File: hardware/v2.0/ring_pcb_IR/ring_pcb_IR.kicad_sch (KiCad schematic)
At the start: 18 parts, among them Q1 Q_PNP_BEC, Q2 Q_Dual_NPN_NPN_C2E2C1E1B1B2, Q3 Q_Dual_NPN_NPN_C2E2C1E1B1B2, U2 ATtiny85-20M

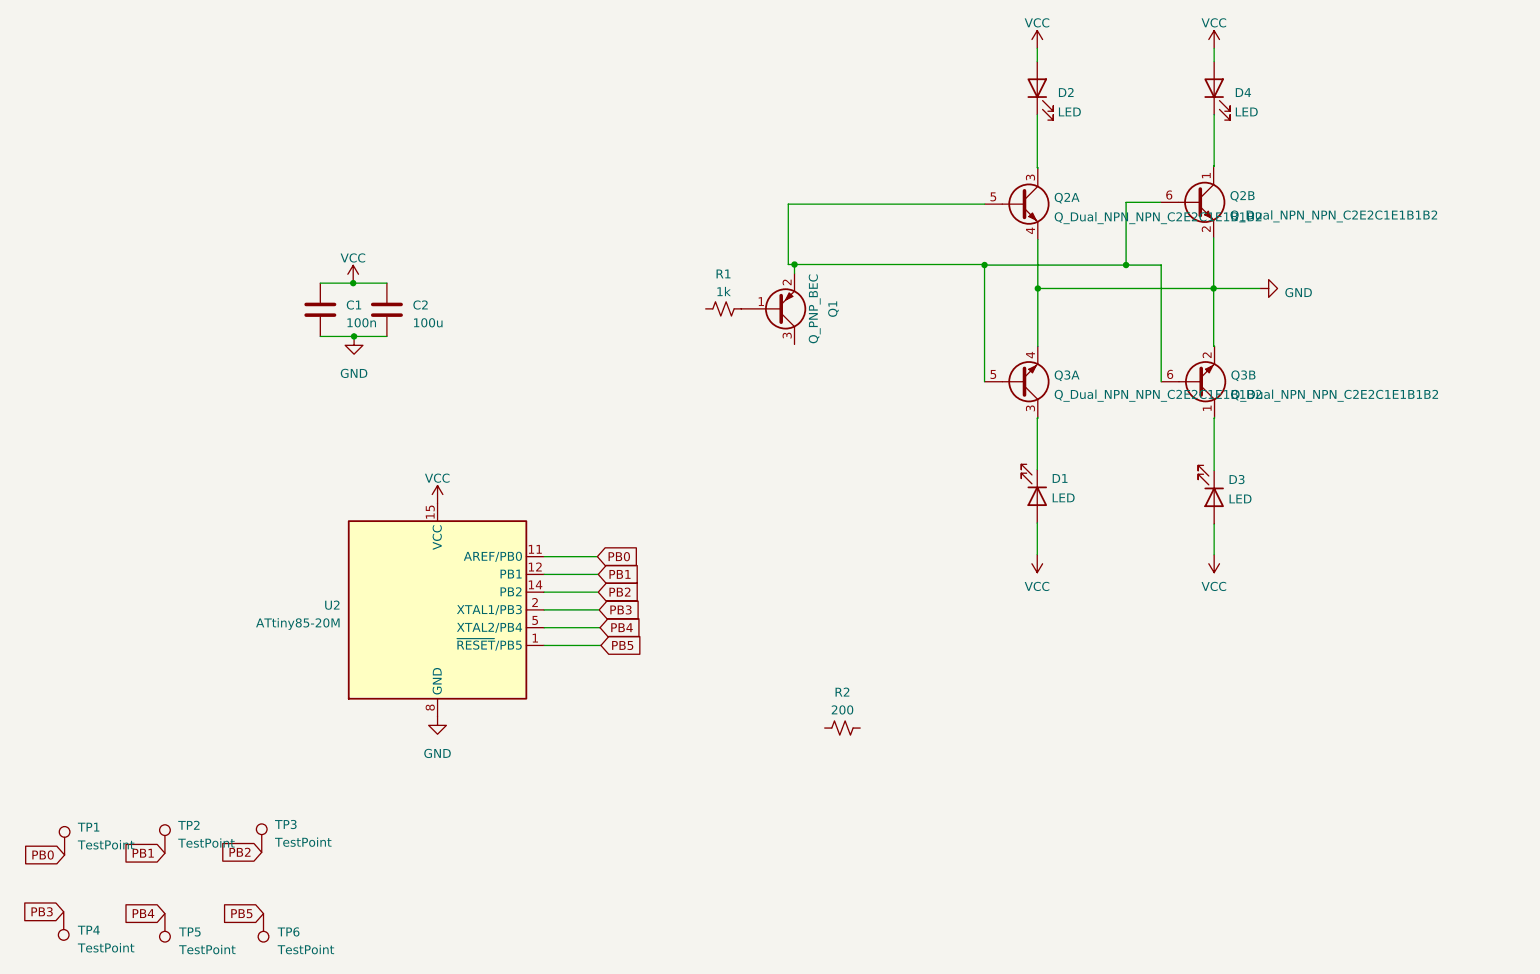
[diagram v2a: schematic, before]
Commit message: Add more wiring for LED and power pads
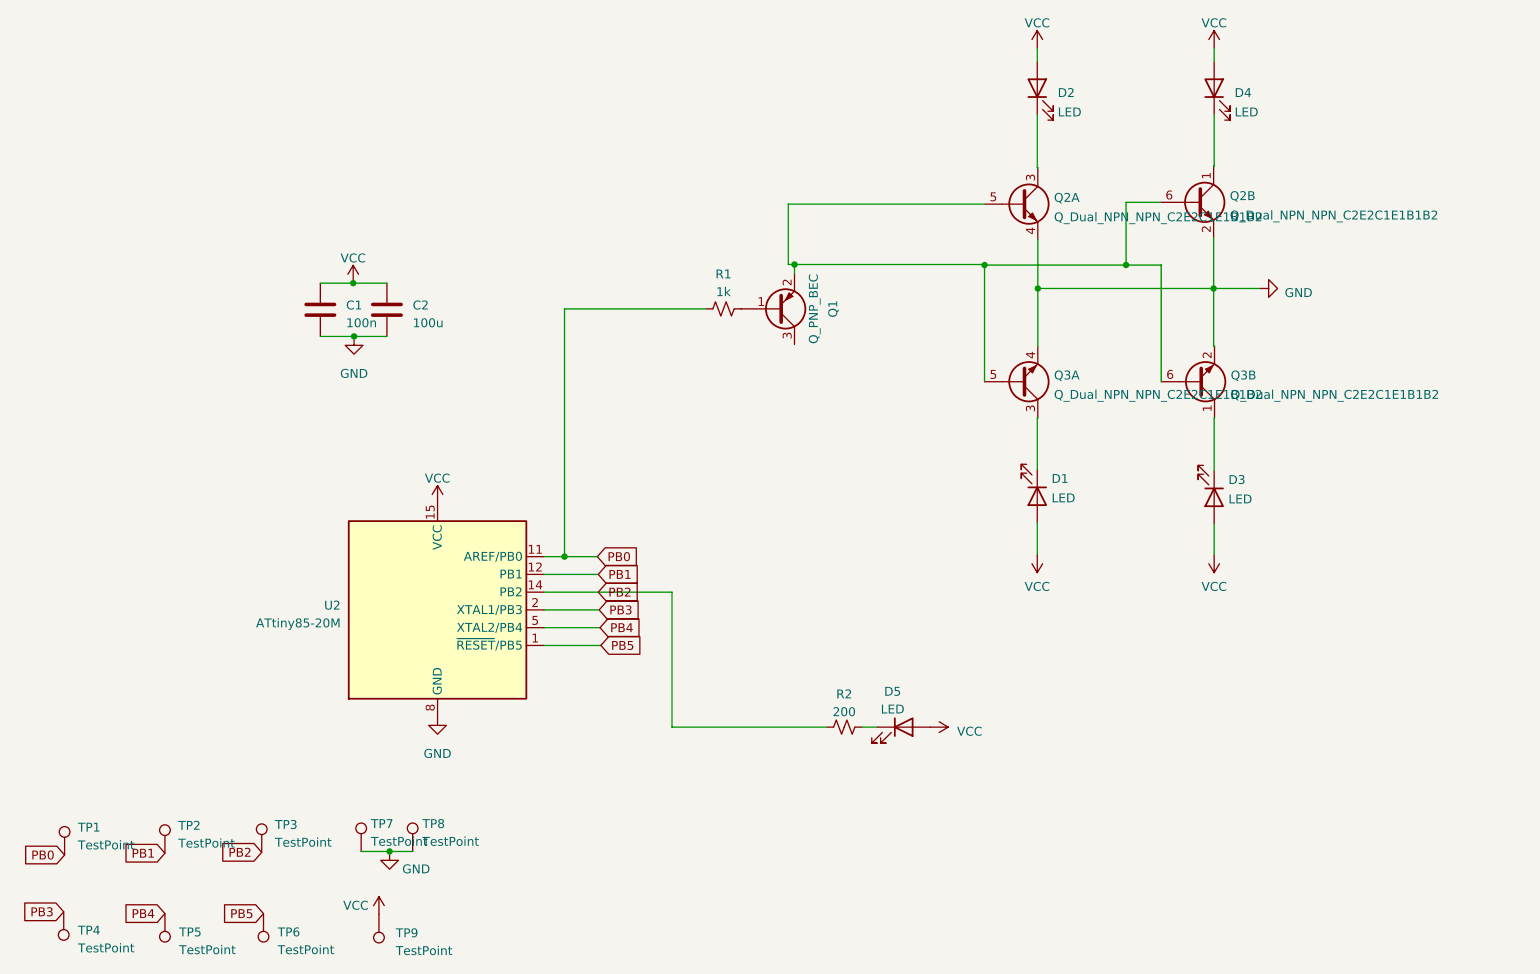
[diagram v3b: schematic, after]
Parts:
- added D5: LED, LED_SMD:LED_0603_1608Metric, symbol Device:LED
- added TP7, TP8, TP9: TestPoint, TestPoint:TestPoint_Pad_1.0x1.0mm, symbol Connector:TestPoint
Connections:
- net GND: now also TP7.1, TP8.1
- net PB0: now also R1.1
- net PB2: now also R2.2
- net VCC: now also D5.2 (A), TP9.1
- net at R2.1: now also D5.1 (K)
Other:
- moved on the sheet: R2
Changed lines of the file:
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@@
   (junction (at 100.33 57.15) (diameter 0) (color 0 0 0 0)
   )
+  (junction (at 105.537 138.43) (diameter 0) (color 0 0 0 0)
+  )
   (junction (at 100.457 64.77) (diameter 0) (color 0 0 0 0)
   )
@@
   (junction (at 163.449 54.483) (diameter 0) (color 0 0 0 0)
   )
+  (junction (at 130.556 96.266) (diameter 0) (color 0 0 0 0)
+  )
   (wire (pts (xy 198.247 40.64) (xy 198.247 40.767))
     (stroke (width 0) (type default))
@@
     (stroke (width 0) (type default))
   )
+  (wire (pts (xy 173.101 120.65) (xy 175.26 120.65))
+    (stroke (width 0) (type default))
+  )
   (wire (pts (xy 223.4692 76.454) (xy 223.4692 83.9724))
     (stroke (width 0) (type default))
@@
     (stroke (width 0) (type default))
   )
-  (wire (pts (xy 127.635 101.346) (xy 135.382 101.346))
+  (wire (pts (xy 127.635 101.346) (xy 145.923 101.346))
+    (stroke (width 0) (type default))
+  )
+  (wire (pts (xy 130.556 96.266) (xy 135.255 96.266))
     (stroke (width 0) (type default))
   )
@@
     (stroke (width 0) (type default))
   )
+  (wire (pts (xy 130.556 60.833) (xy 130.556 96.266))
+    (stroke (width 0) (type default))
+  )
   (wire (pts (xy 127.635 98.806) (xy 135.382 98.806))
     (stroke (width 0) (type default))
@@
     (stroke (width 0) (type default))
   )
-  (wire (pts (xy 127.635 96.266) (xy 135.255 96.266))
+  (wire (pts (xy 127.635 96.266) (xy 130.556 96.266))
     (stroke (width 0) (type default))
   )
@@
     (stroke (width 0) (type default))
   )
+  (wire (pts (xy 168.021 120.65) (xy 145.923 120.65))
+    (stroke (width 0) (type default))
+  )
   (wire (pts (xy 210.8708 54.5592) (xy 190.627 54.5592))
     (stroke (width 0) (type default))
@@
     (stroke (width 0) (type default))
   )
+  (wire (pts (xy 101.473 138.43) (xy 105.537 138.43))
+    (stroke (width 0) (type default))
+  )
+  (wire (pts (xy 145.923 120.65) (xy 145.923 101.346))
+    (stroke (width 0) (type default))
+  )
   (wire (pts (xy 210.8708 45.593) (xy 210.8708 54.5592))
     (stroke (width 0) (type default))
@@
     (stroke (width 0) (type default))
   )
+  (wire (pts (xy 150.749 60.833) (xy 130.556 60.833))
+    (stroke (width 0) (type default))
+  )
   (wire (pts (xy 223.4692 23.5712) (xy 223.4692 25.4508))
     (stroke (width 0) (type default))
@@
   )
   (wire (pts (xy 198.247 76.327) (xy 198.247 76.454))
+    (stroke (width 0) (type default))
+  )
+  (wire (pts (xy 105.537 138.43) (xy 108.839 138.43))
     (stroke (width 0) (type default))
   )
@@
     )
   )
+  (symbol (lib_id "Connector:TestPoint") (at 108.839 138.43 0) (unit 1)
+    (in_bom yes) (on_board yes) (dnp no) (fields_autoplaced)
+    (property "Reference" "TP8" (at 110.236 134.493 0)
+      (effects (font (size 1.27 1.27)) (justify left))
+    )
+    (property "Value" "TestPoint" (at 110.236 137.033 0)
+      (effects (font (size 1.27 1.27)) (justify left))
+    )
+    (property "Footprint" "TestPoint:TestPoint_Pad_1.0x1.0mm" (at 113.919 138.43 0)
+      (effects (font (size 1.27 1.27)) hide)
+    )
+    (property "Datasheet" "~" (at 113.919 138.43 0)
+      (effects (font (size 1.27 1.27)) hide)
+    )
+    (pin "1")
+    (instances
+      (project "ring_pcb_IR"
+        (path "/e63e39d7-6ac0-4ffd-8aa3-1841a4541b55"
+          (reference "TP8") (unit 1)
+        )
+      )
+    )
+  )
   (symbol (lib_id "Connector:TestPoint") (at 87.503 147.32 180) (unit 1)
     (in_bom yes) (on_board yes) (dnp no) (fields_autoplaced)
@@
         (path "/e63e39d7-6ac0-4ffd-8aa3-1841a4541b55"
           (reference "TP6") (unit 1)
+        )
+      )
+    )
+  )
+  (symbol (lib_id "Device:LED") (at 179.07 120.65 0) (unit 1)
+    (in_bom yes) (on_board yes) (dnp no) (fields_autoplaced)
+    (property "Reference" "D5" (at 177.4825 115.57 0)
+      (effects (font (size 1.27 1.27)))
+    )
+    (property "Value" "LED" (at 177.4825 118.11 0)
+      (effects (font (size 1.27 1.27)))
+    )
+    (property "Footprint" "LED_SMD:LED_0603_1608Metric" (at 179.07 120.65 0)
+      (effects (font (size 1.27 1.27)) hide)
+    )
+    (property "Datasheet" "~" (at 179.07 120.65 0)
+      (effects (font (size 1.27 1.27)) hide)
+    )
+    (pin "1")
+    (pin "2")
+    (instances
+      (project "ring_pcb_IR"
+        (path "/e63e39d7-6ac0-4ffd-8aa3-1841a4541b55"
+          (reference "D5") (unit 1)
+        )
+      )
+    )
+  )
+  (symbol (lib_id "Connector:TestPoint") (at 101.473 138.43 0) (unit 1)
+    (in_bom yes) (on_board yes) (dnp no) (fields_autoplaced)
+    (property "Reference" "TP7" (at 102.87 134.493 0)
+      (effects (font (size 1.27 1.27)) (justify left))
+    )
+    (property "Value" "TestPoint" (at 102.87 137.033 0)
+      (effects (font (size 1.27 1.27)) (justify left))
+    )
+    (property "Footprint" "TestPoint:TestPoint_Pad_1.0x1.0mm" (at 106.553 138.43 0)
+      (effects (font (size 1.27 1.27)) hide)
+    )
+    (property "Datasheet" "~" (at 106.553 138.43 0)
+      (effects (font (size 1.27 1.27)) hide)
+    )
+    (pin "1")
+    (instances
+      (project "ring_pcb_IR"
+        (path "/e63e39d7-6ac0-4ffd-8aa3-1841a4541b55"
+          (reference "TP7") (unit 1)
         )
       )
@@
     )
   )
+  (symbol (lib_id "Connector:TestPoint") (at 104.013 147.447 180) (unit 1)
+    (in_bom yes) (on_board yes) (dnp no) (fields_autoplaced)
+    (property "Reference" "TP9" (at 106.426 150.114 0)
+      (effects (font (size 1.27 1.27)) (justify right))
+    )
+    (property "Value" "TestPoint" (at 106.426 152.654 0)
+      (effects (font (size 1.27 1.27)) (justify right))
+    )
+    (property "Footprint" "TestPoint:TestPoint_Pad_1.0x1.0mm" (at 98.933 147.447 0)
+      (effects (font (size 1.27 1.27)) hide)
+    )
+    (property "Datasheet" "~" (at 98.933 147.447 0)
+      (effects (font (size 1.27 1.27)) hide)
+    )
+    (pin "1")
+    (instances
+      (project "ring_pcb_IR"
+        (path "/e63e39d7-6ac0-4ffd-8aa3-1841a4541b55"
+          (reference "TP9") (unit 1)
+        )
+      )
+    )
+  )
   (symbol (lib_id "Device:Q_Dual_NPN_NPN_C2E2C1E1B1B2") (at 220.98 71.247 0) (mirror x) (unit 2)
     (in_bom yes) (on_board yes) (dnp no) (fields_autoplaced)
@@
     )
   )
-  (symbol (lib_id "Device:R_Small_US") (at 170.307 120.777 90) (unit 1)
-    (in_bom yes) (on_board yes) (dnp no) (fields_autoplaced)
-    (property "Reference" "R2" (at 170.307 115.697 90)
-      (effects (font (size 1.27 1.27)))
-    )
-    (property "Value" "200" (at 170.307 118.237 90)
-      (effects (font (size 1.27 1.27)))
-    )
-    (property "Footprint" "Resistor_SMD:R_0603_1608Metric" (at 170.307 120.777 0)
-      (effects (font (size 1.27 1.27)) hide)
-    )
-    (property "Datasheet" "~" (at 170.307 120.777 0)
+  (symbol (lib_id "Device:R_Small_US") (at 170.561 120.65 270) (unit 1)
+    (in_bom yes) (on_board yes) (dnp no) (fields_autoplaced)
+    (property "Reference" "R2" (at 170.561 115.951 90)
+      (effects (font (size 1.27 1.27)))
+    )
+    (property "Value" "200" (at 170.561 118.491 90)
+      (effects (font (size 1.27 1.27)))
+    )
+    (property "Footprint" "Resistor_SMD:R_0603_1608Metric" (at 170.561 120.65 0)
+      (effects (font (size 1.27 1.27)) hide)
+    )
+    (property "Datasheet" "~" (at 170.561 120.65 0)
       (effects (font (size 1.27 1.27)) hide)
     )
@@
     )
   )
+  (symbol (lib_name "VCC_3") (lib_id "power:VCC") (at 104.013 147.447 0) (unit 1)
+    (in_bom yes) (on_board yes) (dnp no)
+    (property "Reference" "#PWR07" (at 104.013 151.257 0)
+      (effects (font (size 1.27 1.27)) hide)
+    )
+    (property "Value" "VCC" (at 100.711 146.177 0)
+      (effects (font (size 1.27 1.27)))
+    )
+    (property "Footprint" "" (at 104.013 147.447 0)
+      (effects (font (size 1.27 1.27)) hide)
+    )
+    (property "Datasheet" "" (at 104.013 147.447 0)
+      (effects (font (size 1.27 1.27)) hide)
+    )
+    (pin "1")
+    (instances
+      (project "ring_pcb_IR"
+        (path "/e63e39d7-6ac0-4ffd-8aa3-1841a4541b55"
+          (reference "#PWR07") (unit 1)
+        )
+      )
+    )
+  )
   (symbol (lib_id "power:VCC") (at 198.1708 96.012 180) (unit 1)
     (in_bom yes) (on_board yes) (dnp no) (fields_autoplaced)
@@
         (path "/e63e39d7-6ac0-4ffd-8aa3-1841a4541b55"
           (reference "D1") (unit 1)
+        )
+      )
+    )
+  )
+  (symbol (lib_name "VCC_2") (lib_id "power:VCC") (at 182.88 120.65 270) (unit 1)
+    (in_bom yes) (on_board yes) (dnp no) (fields_autoplaced)
+    (property "Reference" "#PWR06" (at 179.07 120.65 0)
+      (effects (font (size 1.27 1.27)) hide)
+    )
+    (property "Value" "VCC" (at 186.69 121.285 90)
+      (effects (font (size 1.27 1.27)) (justify left))
+    )
+    (property "Footprint" "" (at 182.88 120.65 0)
+      (effects (font (size 1.27 1.27)) hide)
+    )
+    (property "Datasheet" "" (at 182.88 120.65 0)
+      (effects (font (size 1.27 1.27)) hide)
+    )
+    (pin "1")
+    (instances
+      (project "ring_pcb_IR"
+        (path "/e63e39d7-6ac0-4ffd-8aa3-1841a4541b55"
+          (reference "#PWR06") (unit 1)
         )
       )
@@
         )
       )
+    )
+  )
+  (symbol (lib_id "power:GND") (at 105.537 138.43 0) (unit 1)
+    (in_bom yes) (on_board yes) (dnp no)
+    (property "Reference" "#PWR08" (at 105.537 144.78 0)
+      (effects (font (size 1.27 1.27)) hide)
+    )
+    (property "Value" "GND" (at 109.347 140.97 0)
+      (effects (font (size 1.27 1.27)))
+    )
+    (property "Footprint" "" (at 105.537 138.43 0)
+      (effects (font (size 1.27 1.27)) hide)
+    )
+    (property "Datasheet" "" (at 105.537 138.43 0)
+      (effects (font (size 1.27 1.27)) hide)
+    )
+    (pin "1")
+    (instances
+      (project "ring_pcb_IR"
+        (path "/e63e39d7-6ac0-4ffd-8aa3-1841a4541b55"
+          (reference "#PWR08") (unit 1)
+        )
+      )
